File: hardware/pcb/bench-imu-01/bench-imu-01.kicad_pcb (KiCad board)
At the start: 4 copper layers, 150 x 95 mm, 52 parts, among them J1 USB_C_Receptacle_GCT_USB4105-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, J2 PinHeader_1x04_P2.54mm_Vertic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, J3 PinHeader_1x04_P2.54mm_Vertic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, J4 BarrelJack_CUI_PJ-102AH_Horiz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, M1 TerminalBlock_MaiXu_MX126-5.0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, SW1 SW_PUSH_6mm, U1 LQFP-32_7x7mm_P0.8mm, U2 Bosch_LGA-14_3x2.5mm_P0.5mm, U3 SOT-23-5, U4 SOT-23-6, U5 HTSSOP-24-1EP_4.4x7.8mm_P0.65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, U6 HTSSOP-20-1EP_4.4x6.5mm_P0.65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

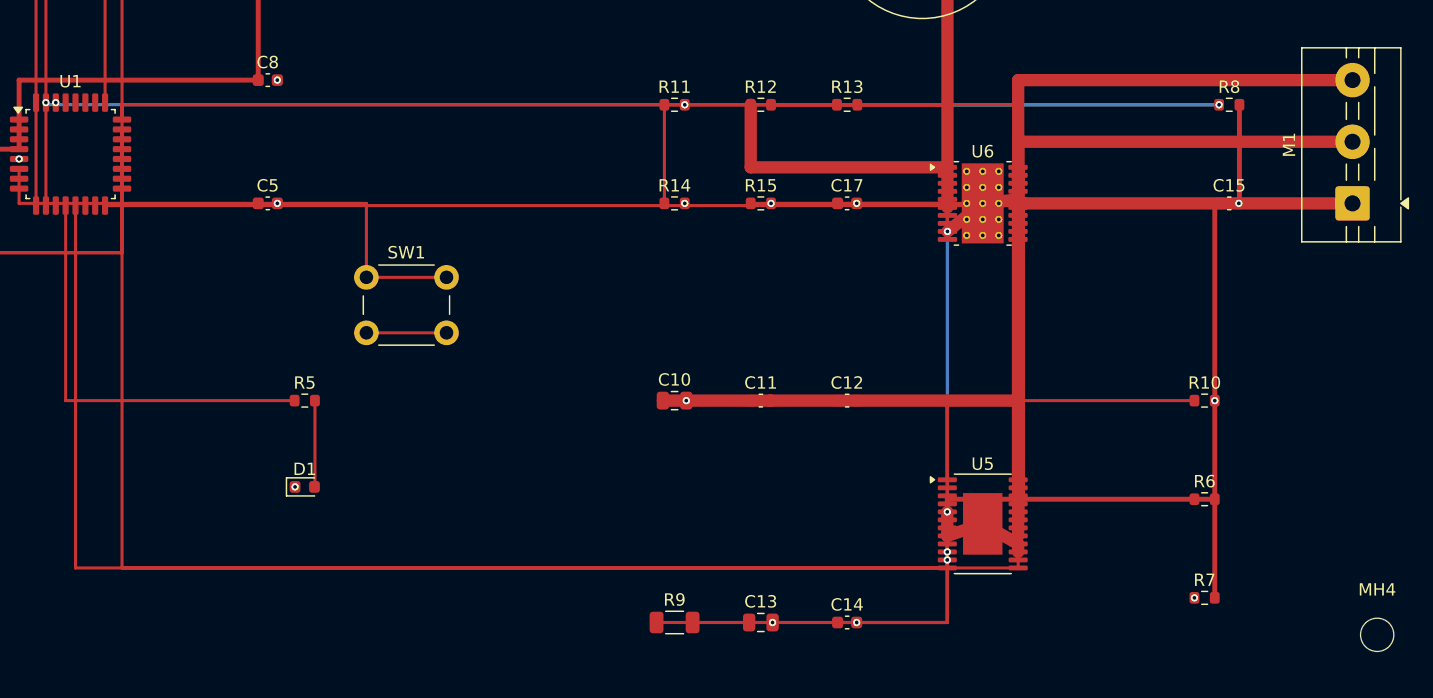
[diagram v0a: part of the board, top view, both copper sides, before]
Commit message: PCB Engineer: fix ISS-031 (HIGH) -- U5 thermal-via array, closing the last half
Continued iteration per Chief Engineer's disposition ("full authority to
keep going here"). Closes the second half of ISS-031 -- the first half
(pin 25/EP missing from the schematic symbol) was already fixed in an
earlier round; this fixes the footprint's lack of a thermal-via array.

Re-read DRV10983's own primary datasheet (SLVSCP6H) this cycle via the
same r.jina.ai text-extraction proxy already used elsewhere in this
project's history, specifically for its Layout Guidelines section (not
previously cited under any Evidence ID): "The exposed thermal pad must be
electrically connected to the ground plane through soldering to PCB for
proper operation and connected to bottom side of PCB through vias for
better thermal spreading," and "Keep the thermal pad connection as large
as possible, both on the bottom side and top side. It should be one
piece of copper without any gaps." Logged as DS-MTR-081 in
datasheets/evidence-log.md -- this is the part's OWN stated requirement,
stronger evidence than the generic SLMA002/SLMA004 PowerPAD app-note
citation the finding originally relied on.

Switched U5's footprint from the prior ASSUMPTION-labeled bare-pad custom
footprint (Package_SO:HTSSOP-24-1EP_4.4x7.8mm_P0.65mm_EP3.2x5mm, no via
array at all) to a real, standard KiCad library footprint
(...EP3.4x7.8mm_Mask2.4x4.68mm_ThermalVias) with an 18-via thermal array
(0.3mm drill / 0.6mm pad, matching the "0.3-0.33mm" guidance the finding
itself cited) and a larger 3.4x7.8mm F.Cu land, better matching the
datasheet's own "as large as possible" directive. Chose a real, vetted
library part over hand-building a custom via array from scratch --
verified all 3 HTSSOP-24-1EP-with-ThermalVias variants in KiCad's library
share the same F.Cu land size and differ only in via/mask sizing; picked
the one whose via drill (0.3mm) most closely matches the cited guidance.

Independently re-verified before marking RESO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
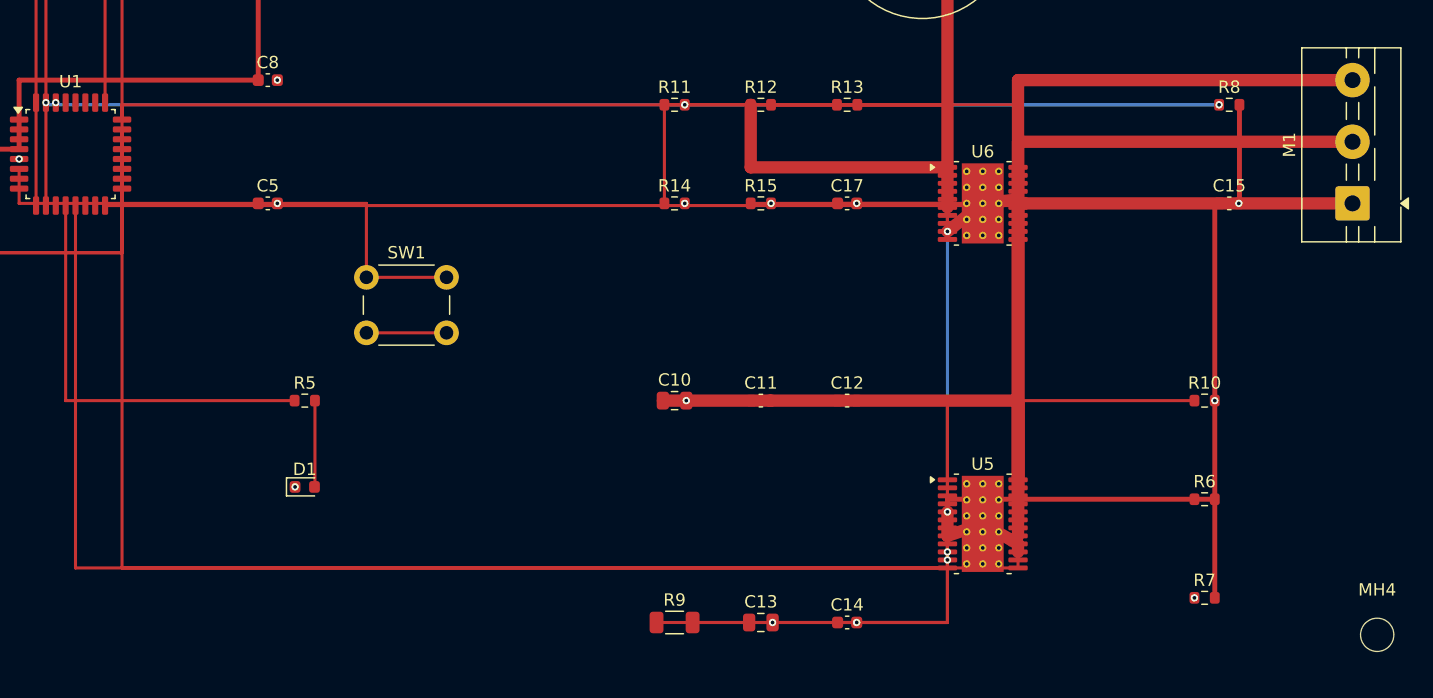
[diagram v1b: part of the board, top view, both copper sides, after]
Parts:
- U5: value HTSSOP-24-1EP_4.4x7.8mm_P0.65mm_EP3.2x5mm -> HTSSOP-24-1EP_4.4x7.8mm_P0.65mm_EP3.4x7.8mm_Mask2.4x4.68mm_ThermalVias; footprint HTSSOP-24-1EP_4.4x7.8mm_P0.65mm_EP3.2x5mm -> HTSSOP-24-1EP_4.4x7.8mm_P0.65mm_EP3.4x7.8mm_Mask2.4x4.68mm_ThermalVias

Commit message: PCB Engineer (at explicit Chief Engineer direction): attempt genuine design fix for ISS-032 (HIGH) -- add F2 GND-leg PTC fuse
Chief Engineer independently audited the CONDITIONAL PR (#17), confirmed
all claims, and gave explicit disposition on the 4 remaining open items:
continue iterating freely on ISS-031/036/037, but for ISS-032 (the
safety-critical J4 GND-hijack finding) -- "take a real crack at this as a
Circuit Engineer-level design question before treating this as an
escalation."

## The problem, precisely

J4 (barrel jack)'s tip/sleeve pin mapping is an ASSUMPTION (primary
datasheet's mechanical drawing not renderable by this session's
tooling). Before this fix: J4 pin1 (assumed sleeve/GND) tied DIRECTLY to
the shared ground net with zero protection, while J4 pin3 (assumed tip/+)
went through F1 (fuse) then D2 (series reverse-polarity diode). D2 only
ever protects against an EXTERNAL failure (a user plugging in a
reverse-polarity supply) -- it sits in the wrong leg to do anything about
an INTERNAL failure, where this design's own pin-mapping assumption is
simply wrong. If pin1/pin3 are actually swapped, the barrel jack's full
+9-13V supply would be applied directly to the shared ground reference
(used by the MCU, IMU, and J1's USB-C GND) with nothing in series to stop
it -- a real, previously undisclosed-as-such safety gap the design
documentation had actually overstated as covered by D2.

## The fix

Added F2: a second Littelfuse 30R500UF PTC resettable fuse, identical in
kind to F1 (same MPN, same DS-PROT-006/032/033 evidence), now in series
between J4's sleeve/GND pin and the shared ground net. This makes the
worst case safe REGARDLESS of which physical pin actually turns out to be
tip vs. sleeve, without ever needing to resolve that ASSUMPTION -- exactly
the property the Chief Engineer asked whether a second protective element
could achieve, and the reviewer's own ISS-032 finding text had already
suggested as an option ("add a second, independent protect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
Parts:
- added F2: Fuse_Littelfuse_30R500UF_Radial_D14.0mm_P10.2mm, Fuse_Littelfuse_30R500UF_Radial_D14.0mm_P10.2mm, F.Cu at (83.0, 8.00)
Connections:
- J4 pad 1: GND -> J4_GND_RAW
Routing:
- net J4_GND_RAW: track 0.00 -> 22.0 mm
- net GND: track 574.0 -> 587.5 mm

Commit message: ISS-036: implement real GND zone fill on In1.Cu (Kyosuke's go-ahead)
Kyosuke woke and explicitly authorized resuming real engineering work on
ISS-036 -- specifically re-investigating option (a) from his own deferral
decision (ECO-033): get a working internal-GND-layer zone fill, since the
Chief Engineer's own independent ZONE_FILLER.Fill() re-test succeeded but
against a different, unrelated F.Cu zone, leaving the real GND-on-In1.Cu
zone untested either way.

Root-caused the segfault precisely instead of treating it as flaky: it
is NOT flaky. pcbnew.ZONE_FILLER.Fill() against this exact zone/board
segfaults 100% of the time (3/3, two different call-site placements
tested within generate_pcb.py's own construction) when called in the
SAME process that incrementally built the board via the pcbnew Python
API. It succeeds 100% of the time (15+ direct calls across this
session's testing) against a board freshly reloaded via
pcbnew.LoadBoard() from an already-saved .kicad_pcb file -- and a
minimal from-scratch reproduction (a single zone, no other complexity)
does not crash in-process either, so this is specific to this real,
complex board's in-memory construction state, not zone-filling in
general. This reconciles the Chief Engineer's own successful re-test
(loaded a saved file) with the original segfault reports (always
in-process) without invoking "non-deterministic."

Fix implemented in generate_pcb.py itself, not a one-off hand patch:
build the board exactly as before (GND still routed as explicit discrete
tracks on In1.Cu, the known-safe baseline, unconditionally -- guarantees
a valid connected board no matter what follows), save it, then reload
that just-written file fresh into a brand new BOARD object and attempt
the fill there. If it succeeds (confirmed via zone.IsFilled(), not just
the return value), remove the now-redundant discrete GND tracks on
In1.Cu (vias stay -- still needed to bring an F.Cu pad down to the zone)
and re-save. Any non-crashing failure falls 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
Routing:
- net GND: track 587.5 -> 61.0 mm
